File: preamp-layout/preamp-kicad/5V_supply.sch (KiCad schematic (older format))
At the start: 20 parts, among them J5 Screw_Terminal_01x02, J6 Conn_01x02_Male, J7 Conn_01x02_Male, J8 Conn_01x02_Male, T2 Transformer_1P_1S, U3 L7805

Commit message: AC PCB Update
Removed Switch symbol from PCB, moved to main sheet. Started playing with footprint assignment. Other minor updates.
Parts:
- renumbered J6 to J10, J7 to J11, J8 to J12, J5 to J9
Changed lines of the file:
@@
 rectified_+
 $Comp
-L Connector:Conn_01x02_Male J6
+L Connector:Conn_01x02_Male J10
 U 1 1 5FD21456
 P 3100 5500
-F 0 "J6" H 3072 5428 50  0000 R CNN
+F 0 "J10" H 3072 5428 50  0000 R CNN
 F 1 "Conn_01x02_Male" H 3072 5383 50  0001 R CNN
 F 2 "" H 3100 5500 50  0001 C CNN
@@
 	2900 5500 2700 5500
 $Comp
-L Connector:Conn_01x02_Male J7
+L Connector:Conn_01x02_Male J11
 U 1 1 5FD3E35C
 P 3100 6100
-F 0 "J7" H 3072 6028 50  0000 R CNN
+F 0 "J11" H 3072 6028 50  0000 R CNN
 F 1 "Conn_01x02_Male" H 3072 5983 50  0001 R CNN
 F 2 "" H 3100 6100 50  0001 C CNN
@@
 	2900 6100 2700 6100
 $Comp
-L Connector:Conn_01x02_Male J8
+L Connector:Conn_01x02_Male J12
 U 1 1 5FD41D04
 P 3100 6650
-F 0 "J8" H 3072 6578 50  0000 R CNN
+F 0 "J12" H 3072 6578 50  0000 R CNN
 F 1 "Conn_01x02_Male" H 3072 6533 50  0001 R CNN
 F 2 "" H 3100 6650 50  0001 C CNN
@@
 P 1500 3300
 AR Path="/5E27B612/5FD91D86" Ref="J?"  Part="1"
-AR Path="/5E5EF2D4/5FD91D86" Ref="J5"  Part="1"
-F 0 "J5" H 1418 3425 50  0000 C CNN
+AR Path="/5E5EF2D4/5FD91D86" Ref="J9"  Part="1"
+F 0 "J9" H 1418 3425 50  0000 C CNN
 F 1 "Screw_Terminal_01x02" H 1418 3066 50  0001 C CNN
 F 2 "" H 1500 3300 50  0001 C CNN
@@
 $EndComp
 $Comp
-L power:PWR_FLAG #FLG0105
+L power:PWR_FLAG #FLG05
 U 1 1 65AE5699
 P 6500 3100
-F 0 "#FLG0105" H 6500 3175 50  0001 C CNN
+F 0 "#FLG05" H 6500 3175 50  0001 C CNN
 F 1 "PWR_FLAG" H 6500 3273 50  0000 C CNN
 F 2 "" H 6500 3100 50  0001 C CNN
@@
 $EndComp
 $Comp
-L power:PWR_FLAG #FLG0106
+L power:PWR_FLAG #FLG06
 U 1 1 65AE5DC2
 P 8050 3750
-F 0 "#FLG0106" H 8050 3825 50  0001 C CNN
+F 0 "#FLG06" H 8050 3825 50  0001 C CNN
 F 1 "PWR_FLAG" H 8050 3923 50  0000 C CNN
 F 2 "" H 8050 3750 50  0001 C CNN

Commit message: Initial Footprint Assignment
Assigned footprints to SMT resistors, pin headers, screw terminals, LEDs, DIP-8 ICs
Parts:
- D9: footprint (none) -> LED_SMD:LED_1206_3216Metric_Pad1.42x1.75mm_HandSolder
- J10, J11, J12: footprint (none) -> Connector_PinHeader_2.54mm:PinHeader_1x02_P2.54mm_Vertical
- R8: footprint (none) -> Resistor_SMD:R_1206_3216Metric_Pad1.42x1.75mm_HandSolder
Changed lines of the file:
@@
 F 0 "R8" V 4193 6100 50  0000 C CNN
 F 1 "10K" V 4284 6100 50  0000 C CNN
-F 2 "" V 4330 6100 50  0001 C CNN
+F 2 "Resistor_SMD:R_1206_3216Metric_Pad1.42x1.75mm_HandSolder" V 4330 6100 50  0001 C CNN
 F 3 "~" H 4400 6100 50  0001 C CNN
 	1    4400 6100
@@
 F 0 "D9" V 4439 6383 50  0000 R CNN
 F 1 "LED" V 4348 6383 50  0000 R CNN
-F 2 "" H 4400 6500 50  0001 C CNN
+F 2 "LED_SMD:LED_1206_3216Metric_Pad1.42x1.75mm_HandSolder" H 4400 6500 50  0001 C CNN
 F 3 "~" H 4400 6500 50  0001 C CNN
 	1    4400 6500
@@
 F 0 "J10" H 3072 5428 50  0000 R CNN
 F 1 "Conn_01x02_Male" H 3072 5383 50  0001 R CNN
-F 2 "" H 3100 5500 50  0001 C CNN
+F 2 "Connector_PinHeader_2.54mm:PinHeader_1x02_P2.54mm_Vertical" H 3100 5500 50  0001 C CNN
 F 3 "~" H 3100 5500 50  0001 C CNN
 	1    3100 5500
@@
 F 0 "J11" H 3072 6028 50  0000 R CNN
 F 1 "Conn_01x02_Male" H 3072 5983 50  0001 R CNN
-F 2 "" H 3100 6100 50  0001 C CNN
+F 2 "Connector_PinHeader_2.54mm:PinHeader_1x02_P2.54mm_Vertical" H 3100 6100 50  0001 C CNN
 F 3 "~" H 3100 6100 50  0001 C CNN
 	1    3100 6100
@@
 F 0 "J12" H 3072 6578 50  0000 R CNN
 F 1 "Conn_01x02_Male" H 3072 6533 50  0001 R CNN
-F 2 "" H 3100 6650 50  0001 C CNN
+F 2 "Connector_PinHeader_2.54mm:PinHeader_1x02_P2.54mm_Vertical" H 3100 6650 50  0001 C CNN
 F 3 "~" H 3100 6650 50  0001 C CNN
 	1    3100 6650

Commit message: BOM update
Minor changes to schematic, value changes and footprint entry. BOM updated with parts sourcing
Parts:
- D10: value D -> SM4001
- D11: value 1N4004 -> SM4001
- J10, J11, J12: footprint Connector_PinHeader_2.54mm:PinHeader_1x02_P2.54mm_Vertical -> Connector_PinSocket_2.54mm:PinSocket_1x02_P2.54mm_Vertical
- R10: value 240R 1% -> 240R
- R8: value 10K -> 430
- RV3: value R_POT_US -> 5k
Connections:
- wire segments 74 -> 72
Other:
- moved on the sheet: D8, F3, J9
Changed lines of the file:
@@
 AR Path="/5E27B612/5FCCFC72" Ref="D?"  Part="1"
 AR Path="/5E5EF2D4/5FCCFC72" Ref="D10"  Part="1"
-F 0 "D10" V 7754 2729 50  0000 L CNN
-F 1 "D" V 7845 2729 50  0000 L CNN
+F 0 "D10" H 7800 2866 50  0000 C CNN
+F 1 "SM4001" H 7800 2775 50  0000 C CNN
 F 2 "" H 7800 2650 50  0001 C CNN
 F 3 "~" H 7800 2650 50  0001 C CNN
@@
 AR Path="/5E5EF2D4/5FCCFC8B" Ref="R10"  Part="1"
 F 0 "R10" H 8370 3746 50  0000 L CNN
-F 1 "240R 1%" H 8370 3655 50  0000 L CNN
+F 1 "240R" H 8370 3655 50  0000 L CNN
 F 2 "" V 8230 3700 50  0001 C CNN
 F 3 "~" H 8300 3700 50  0001 C CNN
@@
 AR Path="/5E27B612/5FCCFCB8" Ref="C?"  Part="1"
 AR Path="/5E5EF2D4/5FCCFCB8" Ref="C14"  Part="1"
-F 0 "C14" H 7315 3446 50  0000 L CNN
-F 1 "100nF 35V" H 7315 3355 50  0000 L CNN
+F 0 "C14" H 7086 3446 50  0000 R CNN
+F 1 "100nF 35V" H 7086 3355 50  0000 R CNN
 F 2 "" H 7238 3250 50  0001 C CNN
 F 3 "~" H 7200 3400 50  0001 C CNN
@@
 AR Path="/5E27B612/5FCCFD3B" Ref="R?"  Part="1"
 AR Path="/5E5EF2D4/5FCCFD3B" Ref="R8"  Part="1"
-F 0 "R8" V 4193 6100 50  0000 C CNN
-F 1 "10K" V 4284 6100 50  0000 C CNN
+F 0 "R8" H 4470 6146 50  0000 L CNN
+F 1 "430" H 4470 6055 50  0000 L CNN
 F 2 "Resistor_SMD:R_1206_3216Metric_Pad1.42x1.75mm_HandSolder" V 4330 6100 50  0001 C CNN
 F 3 "~" H 4400 6100 50  0001 C CNN
@@
 F 0 "J10" H 3072 5428 50  0000 R CNN
 F 1 "Conn_01x02_Male" H 3072 5383 50  0001 R CNN
-F 2 "Connector_PinHeader_2.54mm:PinHeader_1x02_P2.54mm_Vertical" H 3100 5500 50  0001 C CNN
+F 2 "Connector_PinSocket_2.54mm:PinSocket_1x02_P2.54mm_Vertical" H 3100 5500 50  0001 C CNN
 F 3 "~" H 3100 5500 50  0001 C CNN
 	1    3100 5500
@@
 F 0 "J11" H 3072 6028 50  0000 R CNN
 F 1 "Conn_01x02_Male" H 3072 5983 50  0001 R CNN
-F 2 "Connector_PinHeader_2.54mm:PinHeader_1x02_P2.54mm_Vertical" H 3100 6100 50  0001 C CNN
+F 2 "Connector_PinSocket_2.54mm:PinSocket_1x02_P2.54mm_Vertical" H 3100 6100 50  0001 C CNN
 F 3 "~" H 3100 6100 50  0001 C CNN
 	1    3100 6100
@@
 F 0 "J12" H 3072 6578 50  0000 R CNN
 F 1 "Conn_01x02_Male" H 3072 6533 50  0001 R CNN
-F 2 "Connector_PinHeader_2.54mm:PinHeader_1x02_P2.54mm_Vertical" H 3100 6650 50  0001 C CNN
+F 2 "Connector_PinSocket_2.54mm:PinSocket_1x02_P2.54mm_Vertical" H 3100 6650 50  0001 C CNN
 F 3 "~" H 3100 6650 50  0001 C CNN
 	1    3100 6650
@@
 L Connector:Screw_Terminal_01x02 J?
 U 1 1 5FD91D86
-P 1500 3300
+P 1500 3000
 AR Path="/5E27B612/5FD91D86" Ref="J?"  Part="1"
 AR Path="/5E5EF2D4/5FD91D86" Ref="J9"  Part="1"
-F 0 "J9" H 1418 3425 50  0000 C CNN
-F 1 "Screw_Terminal_01x02" H 1418 3066 50  0001 C CNN
-F 2 "" H 1500 3300 50  0001 C CNN
-F 3 "~" H 1500 3300 50  0001 C CNN
-	1    1500 3300
+F 0 "J9" H 1418 3125 50  0000 C CNN
+F 1 "Screw_Terminal_01x02" H 1418 2766 50  0001 C CNN
+F 2 "" H 1500 3000 50  0001 C CNN
+F 3 "~" H 1500 3000 50  0001 C CNN
+	1    1500 3000
 	-1   0    0    -1
 $EndComp
-Wire Wire Line
-	1700 3300 1800 3300
-Wire Wire Line
-	2100 3300 2100 3150
-Wire Wire Line
-	1700 3400 1900 3400
-Wire Wire Line
-	2100 3400 2100 3550
-Text HLabel 1800 3550 3    50   UnSpc ~ 0
-AC+
-Text HLabel 1900 3550 3    50   UnSpc ~ 0
-AC-
-Wire Wire Line
-	1800 3550 1800 3300
-Connection ~ 1800 3300
-Wire Wire Line
-	1800 3300 2100 3300
-Wire Wire Line
-	1900 3550 1900 3400
-Connection ~ 1900 3400
-Wire Wire Line
-	1900 3400 2100 3400
 $Comp
 L Device:Fuse F?
 U 1 1 5FD91D98
-P 3100 3150
+P 2150 3000
 AR Path="/5E26F6FE/5FD91D98" Ref="F?"  Part="1"
 AR Path="/5E27B612/5FD91D98" Ref="F?"  Part="1"
 AR Path="/5E5EF2D4/5FD91D98" Ref="F3"  Part="1"
-F 0 "F3" V 2903 3150 50  0000 C CNN
-F 1 "Fuse" V 2994 3150 50  0000 C CNN
-F 2 "" V 3030 3150 50  0001 C CNN
-F 3 "~" H 3100 3150 50  0001 C CNN
-	1    3100 3150
+F 0 "F3" V 1953 3000 50  0000 C CNN
+F 1 "Fuse" V 2044 3000 50  0000 C CNN
+F 2 "" V 2080 3000 50  0001 C CNN
+F 3 "~" H 2150 3000 50  0001 C CNN
+	1    2150 3000
 	0    1    1    0
 $EndComp
-Wire Wire Line
-	2900 3150 2950 3150
-Wire Wire Line
-	2900 3550 2950 3550
 $Comp
 L Diode_Bridge:DF02M D?
 U 1 1 5FD91DA0
-P 3600 3350
+P 3750 3050
 AR Path="/5E27B612/5FD91DA0" Ref="D?"  Part="1"
 AR Path="/5E5EF2D4/5FD91DA0" Ref="D8"  Part="1"
-F 0 "D8" H 3944 3396 50  0000 L CNN
-F 1 "DF02M" H 3944 3305 50  0000 L CNN
-F 2 "Diode_THT:Diode_Bridge_DIP-4_W7.62mm_P5.08mm" H 3750 3475 50  0001 L CNN
-F 3 "http://www.vishay.com/docs/88571/dfm.pdf" H 3600 3350 50  0001 C CNN
-	1    3600 3350
-	1    0    0    -1
-$EndComp
-Wire Wire Line
-	2950 3550 2950 3700
-Wire Wire Line
-	2950 3700 3600 3700
-Wire Wire Line
-	3600 3700 3600 3650
-Wire Wire Line
-	3250 3150 3300 3150
-Wire Wire Line
-	3300 3150 3300 3000
-Wire Wire Line
-	3300 3000 3600 3000
-Wire Wire Line
-	3600 3000 3600 3050
-Wire Wire Line
-	3300 3350 3300 3800
-Wire Wire Line
-	3900 3350 3900 3800
-Text Label 3300 3800 3    50   ~ 0
-rectified_-
-Text Label 3900 3800 3    50   ~ 0
-rectified_+
+F 0 "D8" H 4094 3096 50  0000 L CNN
+F 1 "DF02M" H 4094 3005 50  0000 L CNN
+F 2 "Diode_THT:Diode_Bridge_DIP-4_W7.62mm_P5.08mm" H 3900 3175 50  0001 L CNN
+F 3 "http://www.vishay.com/docs/88571/dfm.pdf" H 3750 3050 50  0001 C CNN
+	1    3750 3050
+	1    0    0    -1
+$EndComp
 $Comp
 L Device:Transformer_1P_1S T?
 U 1 1 5FD91DB1
-P 2500 3350
+P 2800 3050
 AR Path="/5E27B612/5FD91DB1" Ref="T?"  Part="1"
 AR Path="/5E5EF2D4/5FD91DB1" Ref="T2"  Part="1"
-F 0 "T2" H 2500 3731 50  0000 C CNN
-F 1 "Transformer_1P_1S" H 2500 3640 50  0000 C CNN
-F 2 "" H 2500 3350 50  0001 C CNN
-F 3 "~" H 2500 3350 50  0001 C CNN
-	1    2500 3350
+F 0 "T2" H 2800 3339 50  0000 C CNN
+F 1 "Transformer_1P_1S" H 2800 3340 50  0001 C CNN
+F 2 "" H 2800 3050 50  0001 C CNN
+F 3 "~" H 2800 3050 50  0001 C CNN
+	1    2800 3050
 	1    0    0    -1
 $EndComp
@@
 U 1 1 5FD9ED8B
 P 7800 4000
-F 0 "RV3" H 7733 4046 50  0000 R CNN
-F 1 "R_POT_US" H 7733 3955 50  0000 R CNN
+F 0 "RV3" H 7732 4046 50  0000 R CNN
+F 1 "5k" H 7732 3955 50  0000 R CNN
 F 2 "" H 7800 4000 50  0001 C CNN
 F 3 "~" H 7800 4000 50  0001 C CNN
@@
 AR Path="/5E5EF2D4/5FCCFC5A" Ref="D11"  Part="1"
 F 0 "D11" V 8804 3779 50  0000 L CNN
-F 1 "1N4004" V 8895 3779 50  0000 L CNN
+F 1 "SM4001" V 8895 3779 50  0000 L CNN
 F 2 "" H 8850 3700 50  0001 C CNN
 F 3 "~" H 8850 3700 50  0001 C CNN
@@
 $EndComp
 Connection ~ 8050 3750
+Wire Wire Line
+	2400 3000 2400 2850
+Wire Wire Line
+	2400 3100 2400 3250
+Text HLabel 1850 2900 1    50   UnSpc ~ 0
+AC+
+Text HLabel 1850 3200 3    50   UnSpc ~ 0
+AC-
+Text Label 3450 3650 3    50   ~ 0
+rectified_-
+Text Label 4050 3650 3    50   ~ 0
+rectified_+
+Wire Wire Line
+	1700 3000 1850 3000
+Wire Wire Line
+	1700 3100 1850 3100
+Wire Wire Line
+	1850 2900 1850 3000
+Connection ~ 1850 3000
+Wire Wire Line
+	1850 3100 1850 3200
+Connection ~ 1850 3100
+Wire Wire Line
+	1850 3000 2000 3000
+Wire Wire Line
+	1850 3100 2400 3100
+Wire Wire Line
+	2300 3000 2400 3000
+Wire Wire Line
+	3750 2750 3750 2650
+Wire Wire Line
+	3750 2650 3200 2650
+Wire Wire Line
+	3200 2650 3200 2850
+Wire Wire Line
+	3200 3500 3200 3250
+Wire Wire Line
+	3750 3350 3750 3500
+Wire Wire Line
+	3200 3500 3750 3500
+Wire Wire Line
+	3450 3650 3450 3050
+Wire Wire Line
+	4050 3050 4050 3650
 $EndSCHEMATC

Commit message: power headers updated, slight BOM update
changed footprint on all 5V, +-15V to JST B2B / B3B connectors. All male conns now.
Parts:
- J10, J11, J12: footprint Connector_PinSocket_2.54mm:PinSocket_1x02_P2.54mm_Vertical -> Connector_JST:JST_EH_B2B-EH-A_1x02_P2.50mm_Vertical
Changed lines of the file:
@@
 F 0 "J10" H 3072 5428 50  0000 R CNN
 F 1 "Conn_01x02_Male" H 3072 5383 50  0001 R CNN
-F 2 "Connector_PinSocket_2.54mm:PinSocket_1x02_P2.54mm_Vertical" H 3100 5500 50  0001 C CNN
+F 2 "Connector_JST:JST_EH_B2B-EH-A_1x02_P2.50mm_Vertical" H 3100 5500 50  0001 C CNN
 F 3 "~" H 3100 5500 50  0001 C CNN
 	1    3100 5500
@@
 F 0 "J11" H 3072 6028 50  0000 R CNN
 F 1 "Conn_01x02_Male" H 3072 5983 50  0001 R CNN
-F 2 "Connector_PinSocket_2.54mm:PinSocket_1x02_P2.54mm_Vertical" H 3100 6100 50  0001 C CNN
+F 2 "Connector_JST:JST_EH_B2B-EH-A_1x02_P2.50mm_Vertical" H 3100 6100 50  0001 C CNN
 F 3 "~" H 3100 6100 50  0001 C CNN
 	1    3100 6100
@@
 F 0 "J12" H 3072 6578 50  0000 R CNN
 F 1 "Conn_01x02_Male" H 3072 6533 50  0001 R CNN
-F 2 "Connector_PinSocket_2.54mm:PinSocket_1x02_P2.54mm_Vertical" H 3100 6650 50  0001 C CNN
+F 2 "Connector_JST:JST_EH_B2B-EH-A_1x02_P2.50mm_Vertical" H 3100 6650 50  0001 C CNN
 F 3 "~" H 3100 6650 50  0001 C CNN
 	1    3100 6650

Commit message: Transformer specification
updated schematic, BOM with power transformer info. Other minor schematic tweaks.
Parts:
- removed T2: Transformer_1P_1S, symbol Device:Transformer_1P_1S
- added T2: Transformer_1P_2S, symbol Device:Transformer_1P_2S
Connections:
- wire segments 72 -> 76
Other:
- note added: "120VAC"
- note added: "6.3VAC"
- note added: "7.8VDC"
- moved on the sheet: C12, C13, C14, C15, C16, D10, D11, D8, D9, F3, J10, J11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

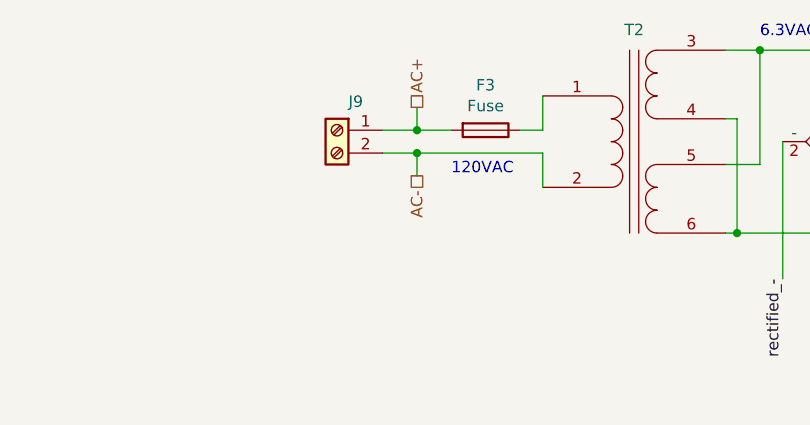
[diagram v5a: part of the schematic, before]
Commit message: screw terminal update
AC power conn update to implement ground. Moved BOM to html file format for web view, not sure if I like it like this but wanted to try it.
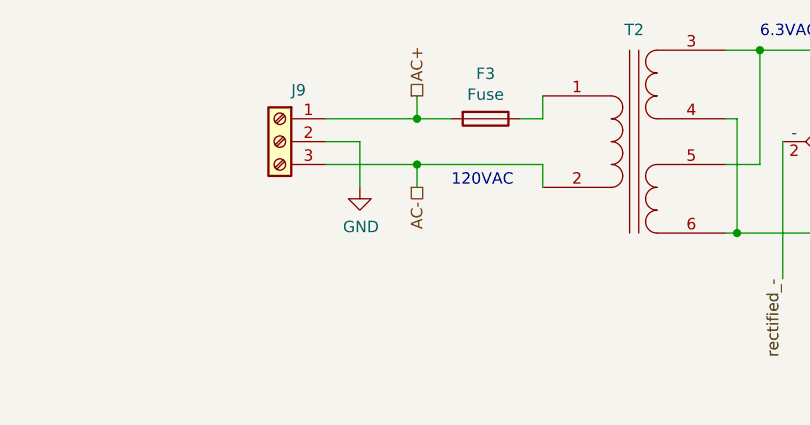
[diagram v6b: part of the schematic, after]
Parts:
- removed J9: Screw_Terminal_01x02, symbol Connector:Screw_Terminal_01x02
- added J9: Screw_Terminal_01x03, TerminalBlock_Phoenix:TerminalBlock_Phoenix_MKDS-3-3-5.08_1x03_P5.08mm_Horizontal, symbol Connector:Screw_Terminal_01x03
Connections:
- net AC+: now also J9.1 (Pin_1)
- net AC-: now also J9.3 (Pin_3)
- net GND: now also J9.2 (Pin_2)
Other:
- moved on the sheet: F3
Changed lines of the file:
@@
-$EndComp
-$Comp
-L Connector:Screw_Terminal_01x02 J?
-U 1 1 5FD91D86
-P 4300 1450
-AR Path="/5E27B612/5FD91D86" Ref="J?"  Part="1"
-AR Path="/5E5EF2D4/5FD91D86" Ref="J9"  Part="1"
-F 0 "J9" H 4218 1575 50  0000 C CNN
-F 1 "Screw_Terminal_01x02" H 4218 1216 50  0001 C CNN
-F 2 "" H 4300 1450 50  0001 C CNN
-F 3 "~" H 4300 1450 50  0001 C CNN
-	1    4300 1450
-	-1   0    0    -1
 $EndComp
 $Comp
 L Device:Fuse F?
 U 1 1 5FD91D98
-P 4950 1450
+P 4950 1400
 AR Path="/5E26F6FE/5FD91D98" Ref="F?"  Part="1"
 AR Path="/5E27B612/5FD91D98" Ref="F?"  Part="1"
 AR Path="/5E5EF2D4/5FD91D98" Ref="F3"  Part="1"
-F 0 "F3" V 4753 1450 50  0000 C CNN
-F 1 "Fuse" V 4844 1450 50  0000 C CNN
-F 2 "" V 4880 1450 50  0001 C CNN
-F 3 "~" H 4950 1450 50  0001 C CNN
-	1    4950 1450
+F 0 "F3" V 4753 1400 50  0000 C CNN
+F 1 "Fuse" V 4844 1400 50  0000 C CNN
+F 2 "" V 4880 1400 50  0001 C CNN
+F 3 "~" H 4950 1400 50  0001 C CNN
+	1    4950 1400
 	0    1    1    0
 $EndComp
@@
 $EndComp
 Connection ~ 6200 4450
-Wire Wire Line
-	5200 1450 5200 1300
-Wire Wire Line
-	5200 1550 5200 1700
-Text HLabel 4650 1350 1    50   UnSpc ~ 0
+Text HLabel 4650 1300 1    50   UnSpc ~ 0
 AC+
-Text HLabel 4650 1650 3    50   UnSpc ~ 0
+Text HLabel 4650 1700 3    50   UnSpc ~ 0
 AC-
 Text Label 6250 2100 3    50   ~ 0
@@
 rectified_+
 Wire Wire Line
-	4500 1450 4650 1450
-Wire Wire Line
-	4500 1550 4650 1550
-Wire Wire Line
-	4650 1350 4650 1450
-Connection ~ 4650 1450
-Wire Wire Line
-	4650 1550 4650 1650
-Connection ~ 4650 1550
-Wire Wire Line
-	4650 1450 4800 1450
-Wire Wire Line
-	4650 1550 5200 1550
-Wire Wire Line
-	5100 1450 5200 1450
+	4650 1300 4650 1400
+Connection ~ 4650 1400
+Wire Wire Line
+	4650 1600 4650 1700
+Connection ~ 4650 1600
+Wire Wire Line
+	4650 1400 4800 1400
+Wire Wire Line
+	4650 1600 5200 1600
+Wire Wire Line
+	5100 1400 5200 1400
 Wire Wire Line
 	6550 1200 6550 1100
@@
 Text Notes 5000 3750 0    50   ~ 0
 7.8VDC
-Text Notes 4800 1650 0    50   ~ 0
+Text Notes 4800 1700 0    50   ~ 0
 120VAC
+$Comp
+L Connector:Screw_Terminal_01x03 J?
+U 1 1 5E8DD1BE
+P 4050 1500
+AR Path="/5E26F6FE/5E8DD1BE" Ref="J?"  Part="1"
+AR Path="/5E5EF2D4/5E8DD1BE" Ref="J9"  Part="1"
+F 0 "J9" H 3968 1725 50  0000 C CNN
+F 1 "Screw_Terminal_01x03" H 3968 1266 50  0001 C CNN
+F 2 "TerminalBlock_Phoenix:TerminalBlock_Phoenix_MKDS-3-3-5.08_1x03_P5.08mm_Horizontal" H 4050 1500 50  0001 C CNN
+F 3 "~" H 4050 1500 50  0001 C CNN
+	1    4050 1500
+	-1   0    0    -1
+$EndComp
+Wire Wire Line
+	5200 1400 5200 1300
+Wire Wire Line
+	5200 1600 5200 1700
+$Comp
+L power:GND #PWR?
+U 1 1 5E8EF23A
+P 4400 1700
+AR Path="/5E26F6FE/5E8EF23A" Ref="#PWR?"  Part="1"
+AR Path="/5E5EF2D4/5E8EF23A" Ref="#PWR?"  Part="1"
+F 0 "#PWR?" H 4400 1450 50  0001 C CNN
+F 1 "GND" H 4405 1527 50  0000 C CNN
+F 2 "" H 4400 1700 50  0001 C CNN
+F 3 "" H 4400 1700 50  0001 C CNN
+	1    4400 1700
+	1    0    0    -1
+$EndComp
+Wire Wire Line
+	4250 1400 4650 1400
+Wire Wire Line
+	4250 1600 4650 1600
+Wire Wire Line
+	4250 1500 4400 1500
+Wire Wire Line
+	4400 1500 4400 1700
 $EndSCHEMATC

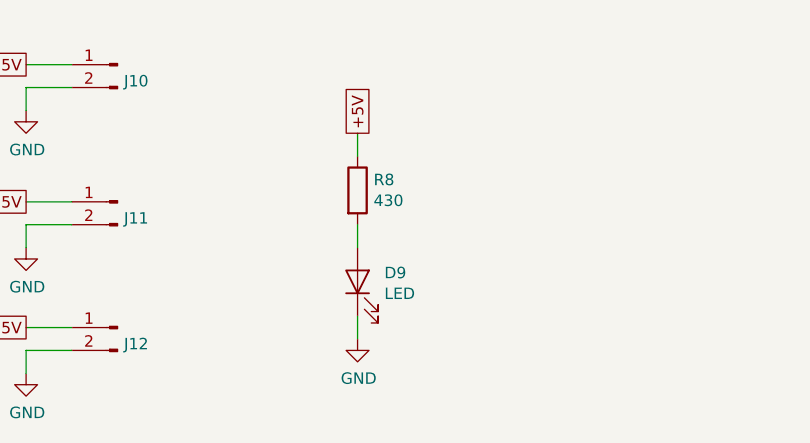
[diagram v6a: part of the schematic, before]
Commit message: Added front panel LED sheet. BOM update. Front panel PCA work
other minor changes like LED color assignments, etc
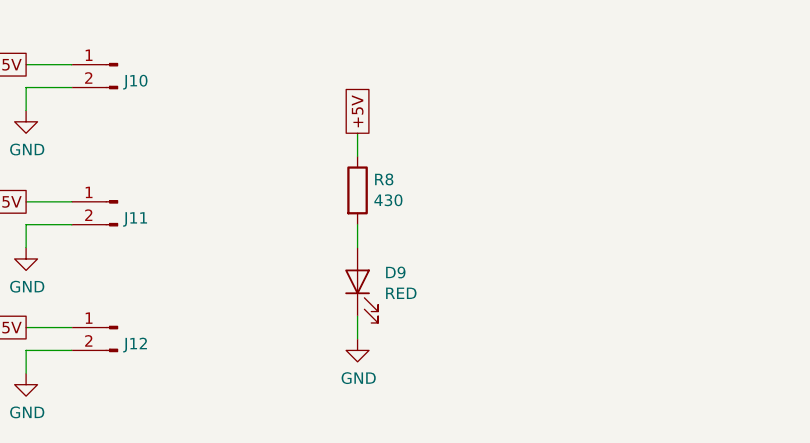
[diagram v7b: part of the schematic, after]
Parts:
- D9: value LED -> RED
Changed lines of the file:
@@
 $Descr A4 11693 8268
 encoding utf-8
-Sheet 4 11
+Sheet 4 12
 Title "5V Power Supply"
 Date "2020-01-23"
@@
 AR Path="/5E27B612/5FCCFD41" Ref="D?"  Part="1"
 AR Path="/5E5EF2D4/5FCCFD41" Ref="D9"  Part="1"
-F 0 "D9" V 3039 6583 50  0000 R CNN
-F 1 "LED" V 2948 6583 50  0000 R CNN
+F 0 "D9" V 3039 6582 50  0000 R CNN
+F 1 "RED" V 2948 6582 50  0000 R CNN
 F 2 "LED_SMD:LED_1206_3216Metric_Pad1.42x1.75mm_HandSolder" H 3000 6700 50  0001 C CNN
 F 3 "~" H 3000 6700 50  0001 C CNN
@@
 P 4400 1700
 AR Path="/5E26F6FE/5E8EF23A" Ref="#PWR?"  Part="1"
-AR Path="/5E5EF2D4/5E8EF23A" Ref="#PWR?"  Part="1"
-F 0 "#PWR?" H 4400 1450 50  0001 C CNN
+AR Path="/5E5EF2D4/5E8EF23A" Ref="#PWR0113"  Part="1"
+F 0 "#PWR0113" H 4400 1450 50  0001 C CNN
 F 1 "GND" H 4405 1527 50  0000 C CNN
 F 2 "" H 4400 1700 50  0001 C CNN

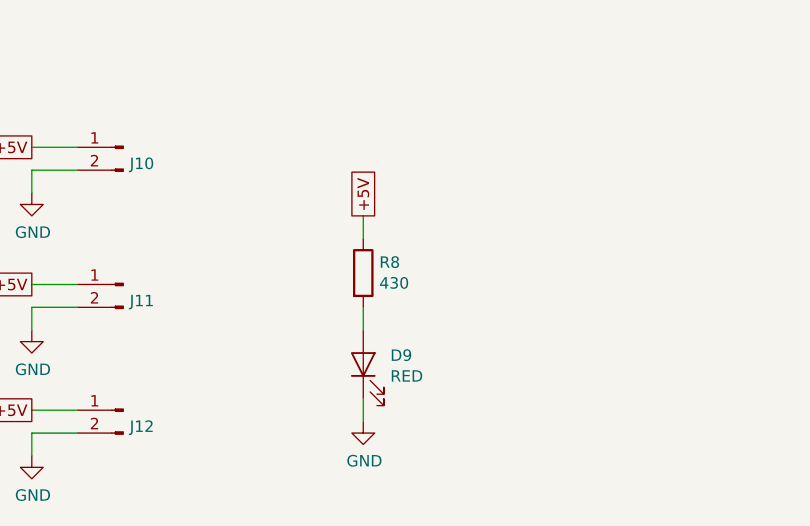
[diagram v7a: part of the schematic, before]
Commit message: LED resistor update
In the process of reviewing layouts and associated parts sourcing, I realized that I had incorrectly calculated the resistors needed for the power supply LEDs on all boards. Updated BOM and schematics to match. Other minor schematic updates.
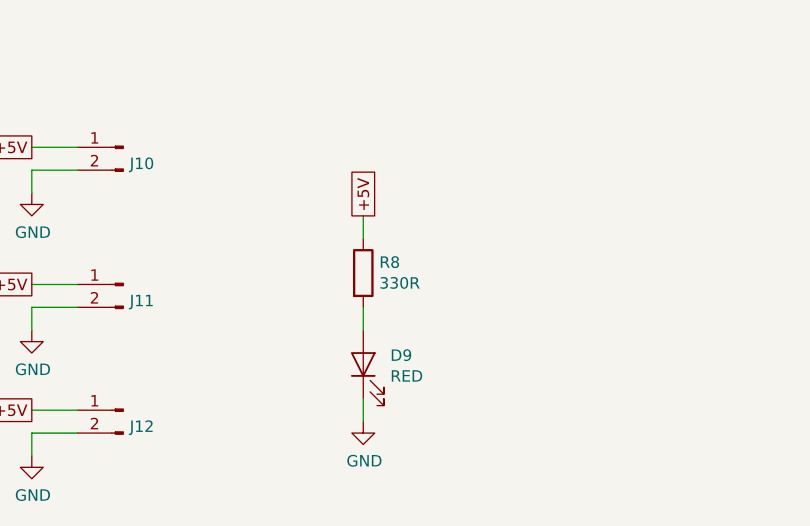
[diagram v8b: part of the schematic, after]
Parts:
- R8: value 430 -> 330R
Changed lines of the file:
@@
 AR Path="/5E5EF2D4/5FCCFD3B" Ref="R8"  Part="1"
 F 0 "R8" H 3070 6346 50  0000 L CNN
-F 1 "430" H 3070 6255 50  0000 L CNN
+F 1 "330R" H 3070 6255 50  0000 L CNN
 F 2 "Resistor_SMD:R_1206_3216Metric_Pad1.42x1.75mm_HandSolder" V 2930 6300 50  0001 C CNN
 F 3 "~" H 3000 6300 50  0001 C CNN
